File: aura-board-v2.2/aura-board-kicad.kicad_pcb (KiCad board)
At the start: 2 copper layers, 76.8 x 53.3 mm, 21 parts, among them J1 Main Power, J2 PWM_3x08, J3 BBCON, J4 Attopilot, J5 GPS, J6 SBUS, J7 Tele, J8 I2C0, U1 TSR2-2450, U2 PocketBeagle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

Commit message: Small labelling tweak.
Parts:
- J4: value Attopilot -> Atto
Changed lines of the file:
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@@
   (layers
     (0 F.Cu signal)
-    (31 B.Cu signal)
+    (31 B.Cu signal hide)
     (32 B.Adhes user)
     (33 F.Adhes user)
@@
   )
   (setup
-    (last_trace_width 0.254)
+    (last_trace_width 0.1524)
     (user_trace_width 0.254)
     (user_trace_width 0.381)
@@
       (effects (font (size 1 1) (thickness 0.15)))
     )
-    (fp_text value Attopilot (at 0 -2.54) (layer F.SilkS)
+    (fp_text value Atto (at 0 -2.54) (layer F.SilkS)
       (effects (font (size 1 1) (thickness 0.15)))
     )
@@
     (at 99.695 79.375 90)
     (descr "2-way 3.5mm pitch terminal block, Phoenix PT series")
-    (fp_text reference J1 (at 1.75 -4.3 90) (layer F.SilkS)
+    (fp_text reference J1 (at 6.35 0 180) (layer F.SilkS)
       (effects (font (size 1 1) (thickness 0.15)))
     )
@@
   (gr_line (start 29.21 102.87) (end 104.775 102.87) (angle 90) (layer Edge.Cuts) (width 0.15))
   (gr_line (start 27.94 49.53) (end 27.94 102.87) (angle 90) (layer Edge.Cuts) (width 0.15))
-  (segment (start 95.25 73.025) (end 97.155 74.93) (width 0.254) (layer F.Cu) (net 1) (status 400000))
-  (segment (start 98.425 79.375) (end 99.695 79.375) (width 0.1524) (layer F.Cu) (net 1) (status 800000))
+  (segment (start 95.25 73.025) (end 97.155 74.93) (width 0.254) (layer F.Cu) (net 1))
+  (segment (start 98.425 79.375) (end 99.695 79.375) (width 0.1524) (layer F.Cu) (net 1))
   (segment (start 97.155 78.105) (end 98.425 79.375) (width 0.254) (layer F.Cu) (net 1))
   (segment (start 97.155 74.93) (end 97.155 78.105) (width 0.254) (layer F.Cu) (net 1))

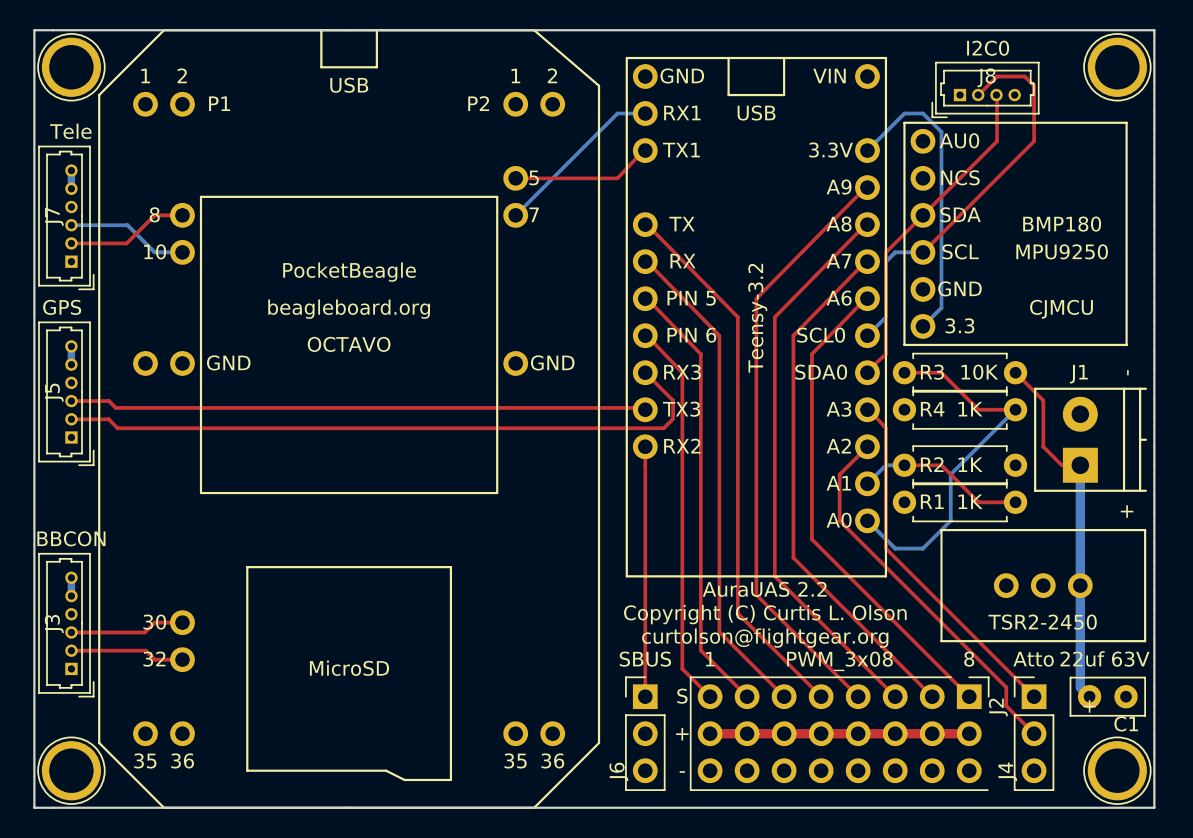
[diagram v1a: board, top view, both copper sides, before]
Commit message: A few small tweaks with labeling.  Nudge one connector and a couple traces.
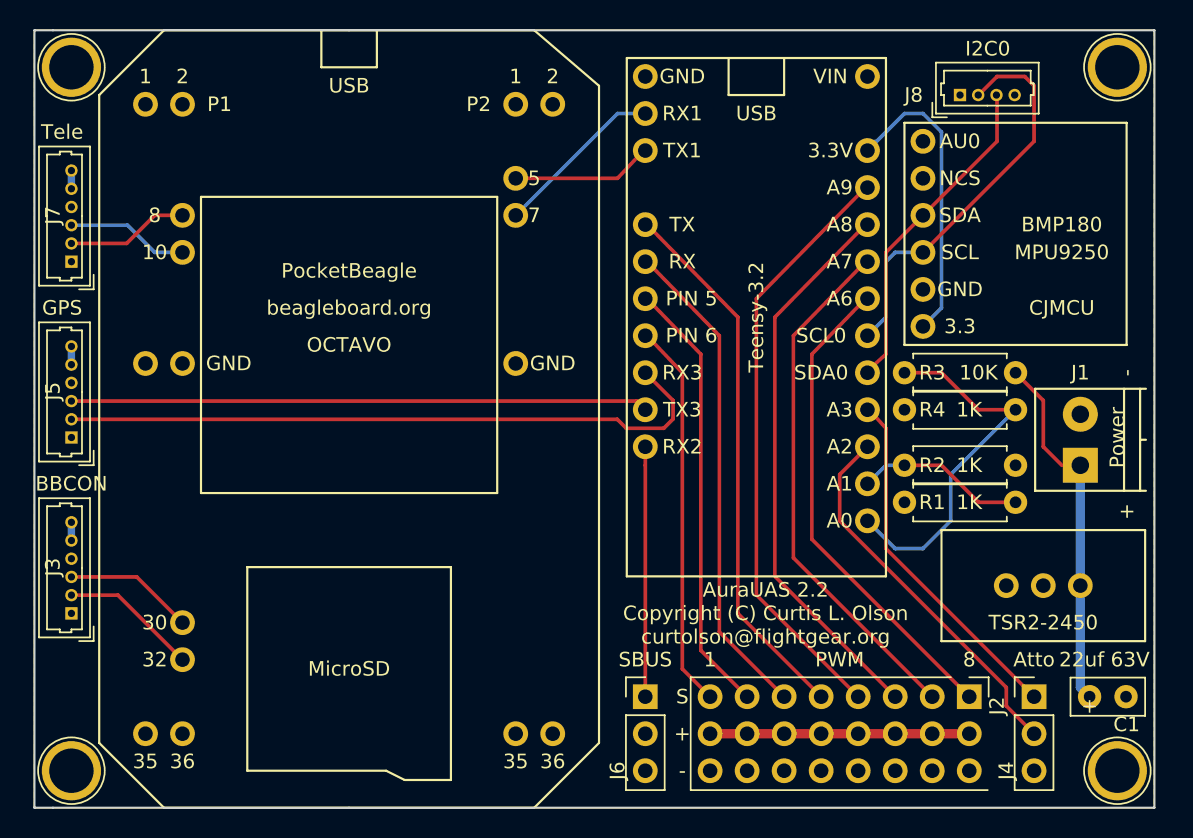
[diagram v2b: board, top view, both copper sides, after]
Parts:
- J1: value Main Power -> Power
- J2: value PWM_3x08 -> PWM
- moved J3 3.81 mm to (30.5, 89.5)
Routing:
- net /UART0_RX: track 7.87 -> 9.45 mm
- net /UART0_TX: track 7.90 -> 8.92 mm
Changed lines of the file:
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@@
     (links 72)
     (no_connects 0)
-    (area 27.702599 48.0946 106.7224 104.3574)
+    (area 27.702599 48.0946 105.012401 104.3574)
     (thickness 1.6)
     (drawings 15)
-    (tracks 122)
+    (tracks 119)
     (zones 0)
     (modules 21)
@@
   )
   (setup
-    (last_trace_width 0.1524)
+    (last_trace_width 0.254)
     (user_trace_width 0.254)
     (user_trace_width 0.381)
@@
   )
   (module Connectors_Molex:Molex_PicoBlade_53047-0610_06x1.25mm_Straight (layer F.Cu)
-    (at 30.48 93.345 90)
+    (at 30.48 89.535 90)
     (descr "Molex PicoBlade, single row, top entry type, through hole, PN:53047-0610")
     (tags "connector molex picoblade")
@@
       (effects (font (size 1 1) (thickness 0.15)))
     )
-    (fp_text value Tele (at 8.89 0 180) (layer F.SilkS)
+    (fp_text value Tele (at 8.89 -0.635 180) (layer F.SilkS)
       (effects (font (size 1 1) (thickness 0.15)))
     )
@@
     (descr "Molex PicoBlade, single row, top entry type, through hole, PN:53047-0410")
     (tags "connector molex picoblade")
-    (fp_text reference J8 (at 1.905 -1.27) (layer F.SilkS)
+    (fp_text reference J8 (at -3.175 0) (layer F.SilkS)
       (effects (font (size 1 1) (thickness 0.15)))
     )
@@
     (fp_line (start -1.9 1.525) (end -1.9 0.525) (layer F.SilkS) (width 0.12))
     (fp_line (start -1.9 1.525) (end -0.9 1.525) (layer F.SilkS) (width 0.12))
-    (fp_text user %R (at -3.175 0) (layer F.Fab)
+    (fp_text user %R (at -3.175 0) (layer F.Fab) hide
       (effects (font (size 1 1) (thickness 0.15)))
     )
@@
       (effects (font (size 1 1) (thickness 0.15)))
     )
-    (fp_text value PWM_3x08 (at -2.54 8.89 360) (layer F.SilkS)
+    (fp_text value PWM (at -2.54 8.89 360) (layer F.SilkS)
       (effects (font (size 1 1) (thickness 0.15)))
     )
@@
       (effects (font (size 1 1) (thickness 0.15)))
     )
-    (fp_text value "Main Power" (at 1.75 6 90) (layer F.Fab)
+    (fp_text value Power (at 1.905 2.54 90) (layer F.SilkS)
       (effects (font (size 1 1) (thickness 0.15)))
     )
@@
   (segment (start 100.33 95.25) (end 99.695 94.615) (width 0.635) (layer B.Cu) (net 1))
   (segment (start 99.695 94.615) (end 99.695 87.63) (width 0.635) (layer B.Cu) (net 1))
-  (segment (start 30.48 87.095) (end 30.48 88.345) (width 0.508) (layer B.Cu) (net 2))
+  (segment (start 30.48 83.285) (end 30.48 84.535) (width 0.508) (layer B.Cu) (net 2) (status 30))
   (segment (start 30.48 71.22) (end 30.48 72.47) (width 0.508) (layer B.Cu) (net 2))
   (segment (start 30.48 59.155) (end 30.48 60.405) (width 0.508) (layer B.Cu) (net 2))
@@
   (segment (start 92.075 95.25) (end 81.28 84.455) (width 0.25) (layer F.Cu) (net 10) (status 10))
   (segment (start 85.09 53.086) (end 85.09 52.578) (width 0.635) (layer B.Cu) (net 11) (status 30))
-  (segment (start 38.1 92.71) (end 36.195 92.71) (width 0.254) (layer F.Cu) (net 12))
-  (segment (start 35.58 92.095) (end 30.48 92.095) (width 0.254) (layer F.Cu) (net 12))
-  (segment (start 36.195 92.71) (end 35.58 92.095) (width 0.254) (layer F.Cu) (net 12))
-  (segment (start 38.1 90.17) (end 36.195 90.17) (width 0.254) (layer F.Cu) (net 13))
-  (segment (start 35.52 90.845) (end 30.48 90.845) (width 0.254) (layer F.Cu) (net 13))
-  (segment (start 36.195 90.17) (end 35.52 90.845) (width 0.254) (layer F.Cu) (net 13))
+  (segment (start 30.48 88.285) (end 33.675 88.285) (width 0.254) (layer F.Cu) (net 12))
+  (segment (start 33.675 88.285) (end 38.1 92.71) (width 0.254) (layer F.Cu) (net 12))
+  (segment (start 30.48 87.035) (end 34.965 87.035) (width 0.254) (layer F.Cu) (net 13))
+  (segment (start 34.965 87.035) (end 38.1 90.17) (width 0.254) (layer F.Cu) (net 13))
   (segment (start 96.52 95.25) (end 86.36 85.09) (width 0.25) (layer F.Cu) (net 15) (status 10))
   (segment (start 86.36 85.09) (end 86.36 76.835) (width 0.25) (layer F.Cu) (net 15))
@@
   (segment (start 96.52 97.79) (end 95.885 97.79) (width 0.254) (layer F.Cu) (net 16))
   (segment (start 69.85 73.025) (end 71.755 74.93) (width 0.254) (layer F.Cu) (net 17))
-  (segment (start 33.04 76.22) (end 30.48 76.22) (width 0.254) (layer F.Cu) (net 17))
-  (segment (start 33.655 76.835) (end 33.04 76.22) (width 0.254) (layer F.Cu) (net 17))
-  (segment (start 71.12 76.835) (end 33.655 76.835) (width 0.254) (layer F.Cu) (net 17))
+  (segment (start 67.925 76.22) (end 30.48 76.22) (width 0.254) (layer F.Cu) (net 17))
+  (segment (start 68.54 76.835) (end 67.925 76.22) (width 0.254) (layer F.Cu) (net 17))
+  (segment (start 71.12 76.835) (end 68.54 76.835) (width 0.254) (layer F.Cu) (net 17))
   (segment (start 71.755 76.2) (end 71.12 76.835) (width 0.254) (layer F.Cu) (net 17))
   (segment (start 71.755 74.93) (end 71.755 76.2) (width 0.254) (layer F.Cu) (net 17))
   (segment (start 69.85 72.898) (end 69.85 73.025) (width 0.254) (layer F.Cu) (net 17) (status 30))
-  (segment (start 69.85 75.438) (end 33.528 75.438) (width 0.254) (layer F.Cu) (net 18) (status 10))
-  (segment (start 33.528 75.438) (end 33.06 74.97) (width 0.254) (layer F.Cu) (net 18))
-  (segment (start 33.06 74.97) (end 30.48 74.97) (width 0.254) (layer F.Cu) (net 18))
+  (segment (start 30.48 74.97) (end 69.255 74.97) (width 0.254) (layer F.Cu) (net 18))
+  (segment (start 69.255 74.97) (end 69.85 75.565) (width 0.254) (layer F.Cu) (net 18))
   (segment (start 69.85 79.375) (end 69.85 77.978) (width 0.25) (layer F.Cu) (net 20) (status 20))
   (segment (start 69.85 95.25) (end 69.85 79.375) (width 0.25) (layer F.Cu) (net 20))

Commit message: Endless tiny tweaks and adjustments continue ...
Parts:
- C1: value 22uf 63V -> 22uf63V
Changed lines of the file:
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@@
   )
   (setup
-    (last_trace_width 0.254)
+    (last_trace_width 0.1524)
     (user_trace_width 0.254)
     (user_trace_width 0.381)
@@
       (effects (font (size 1 1) (thickness 0.15)))
     )
-    (fp_text value "22uf 63V" (at 1.016 -2.54) (layer F.SilkS)
-      (effects (font (size 1 1) (thickness 0.15)))
-    )
+    (fp_text value 22uf63V (at 1.016 -2.54) (layer F.SilkS)
+      (effects (font (size 1 1) (thickness 0.15)))
+    )
